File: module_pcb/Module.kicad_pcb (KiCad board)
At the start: 2 copper layers, 44.4 x 52.7 mm, 29 parts, among them J1 L_SIG_CONN, J2 R_PWR_CONN, J3 R_SIG_CONN, J4 L_PWR_CONN, U1 AMS1117-3.3, U2 TBD62783AFNG, U3 SN74HC595PWR, U4 AMS1117-1.5

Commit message: Layout done
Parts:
- removed H2: MountingHole_Pad, MountingHole:MountingHole_3.2mm_M3_ISO14580_Pad_TopBottom
- moved H3 36.3 mm to (146.3, 110.3)
- moved D2 4.40 mm to (157.5, 96.0)
- moved H1 0.78 mm to (146.3, 82.8)
- moved H4 0.55 mm to (183.2, 82.8)
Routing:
- net Vanode: track 2.61 -> 46.2 mm, vias 0 -> 1
- net Net-(U2-O7): track 0.00 -> 37.7 mm, vias 0 -> 1
- net Net-(U2-O5): track 0.00 -> 36.5 mm, vias 0 -> 1
- net Net-(U2-O2): track 0.00 -> 34.6 mm, vias 0 -> 1
- net Net-(U2-O1): track 0.00 -> 33.6 mm, vias 0 -> 2
- net /GRID_1: track 21.2 -> 52.2 mm, vias 1 -> 3
- net Net-(U2-O8): track 0.00 -> 29.6 mm, vias 0 -> 2
- net /SRCLK: track 25.8 -> 55.3 mm, vias 0 -> 1
- net Net-(U2-O6): track 0.00 -> 28.0 mm, vias 0 -> 2
- net Net-(U2-O4): track 0.00 -> 26.8 mm, vias 0 -> 2
- net Net-(U2-O3): track 0.00 -> 26.2 mm
- net /GRID_2: track 28.0 -> 50.5 mm
- net /RCLK: track 19.1 -> 41.6 mm
- net //SRCLR: track 21.2 -> 41.9 mm, vias 1 -> 2
- net /SER: track 27.3 -> 47.6 mm, vias 1 -> 2
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
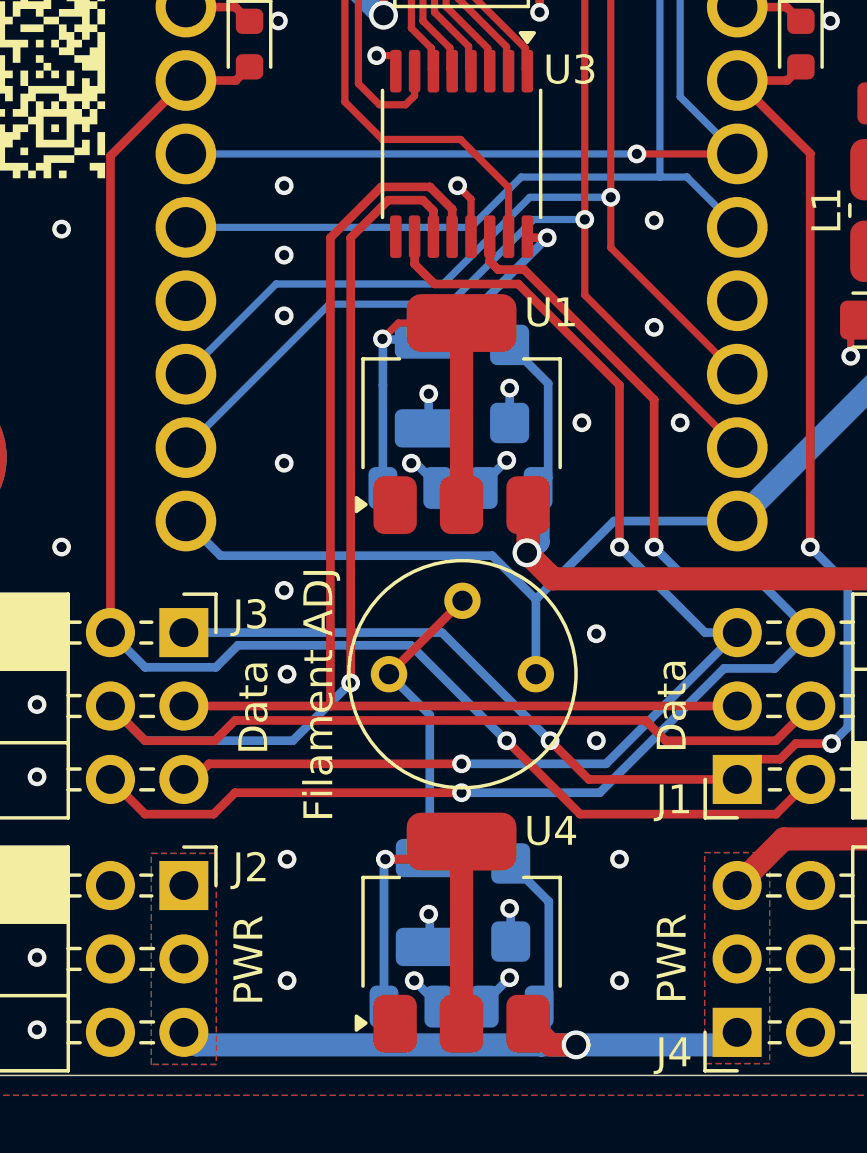
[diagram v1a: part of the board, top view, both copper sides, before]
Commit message: Moved cell battery, generated STEP files
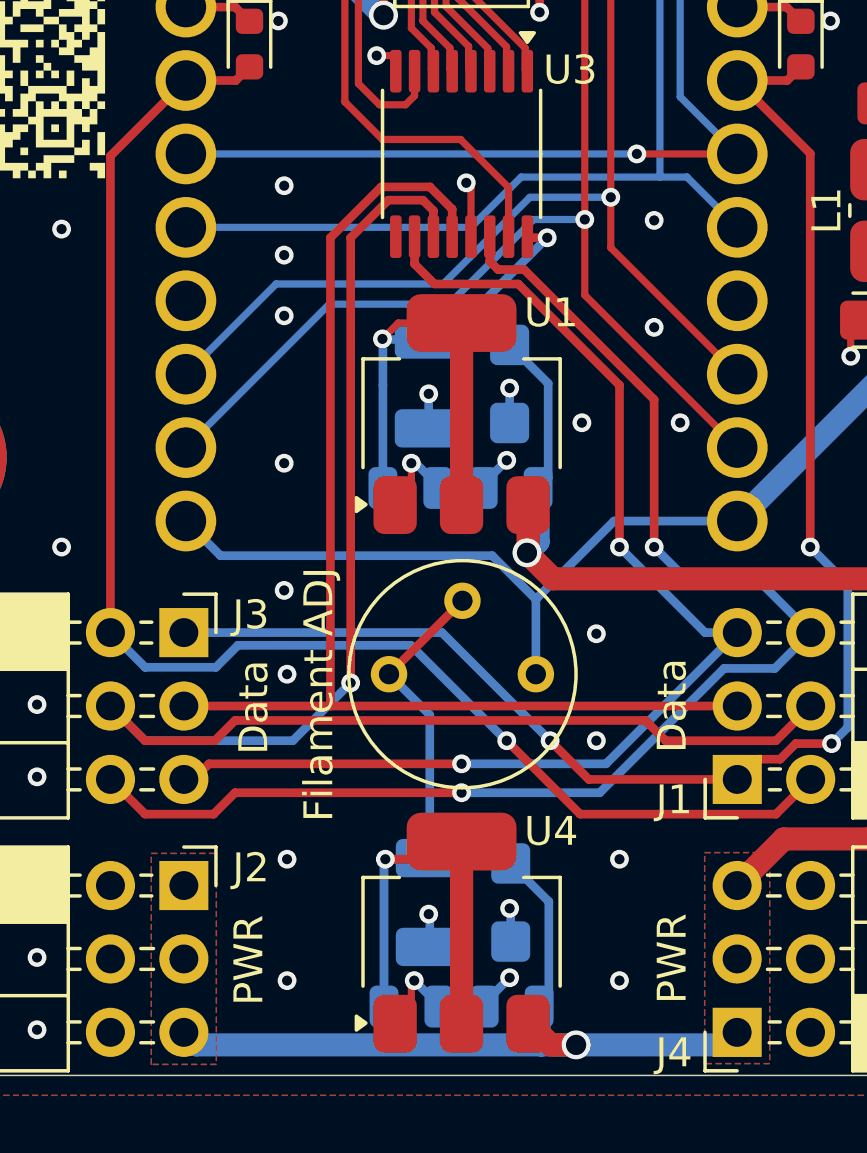
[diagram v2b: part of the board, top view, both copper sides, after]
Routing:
- net GND: track 20.3 -> 23.7 mm
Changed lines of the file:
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@@
+	)
+	(segment
+		(start 162.5375 129.89)
+		(end 163.1 129.3275)
+		(width 0.25)
+		(layer "F.Cu")
+		(net 1)
+	)
+	(segment
+		(start 163.1 129.3275)
+		(end 163.1 128.5)
+		(width 0.25)
+		(layer "F.Cu")
+		(net 1)
 	)
 	(segment
@@
 	)
 	(segment
+		(start 163.1 111.3875)
+		(end 163.1 110.5)
+		(width 0.25)
+		(layer "F.Cu")
+		(net 1)
+	)
+	(segment
 		(start 167.5375 93.94)
 		(end 167.5375 94.9)
@@
 	)
 	(segment
-		(start 165.1625 102.6625)
-		(end 165.1625 101.3625)
+		(start 165.1625 100.9625)
+		(end 165 100.8)
 		(width 0.25)
 		(layer "F.Cu")
@@
 	)
 	(segment
+		(start 162.5375 111.95)
+		(end 163.1 111.3875)
+		(width 0.25)
+		(layer "F.Cu")
+		(net 1)
+	)
+	(segment
 		(start 176.0825 94.72)
 		(end 176.575 95.2125)
@@
 	)
 	(segment
+		(start 163.1 128.5)
+		(end 163.2 128.4)
+		(width 0.25)
+		(layer "F.Cu")
+		(net 1)
+	)
+	(segment
+		(start 165.1625 102.6625)
+		(end 165.1625 100.9625)
+		(width 0.25)
+		(layer "F.Cu")
+		(net 1)
+	)
+	(segment
 		(start 178.3 106.8)
 		(end 178.3 105.88)
-		(width 0.25)
-		(layer "F.Cu")
-		(net 1)
-	)
-	(segment
-		(start 165.1625 101.3625)
-		(end 164.7 100.9)
 		(width 0.25)
 		(layer "F.Cu")
@@
 	)
 	(via
-		(at 164.7 100.9)
-		(size 0.65)
-		(drill 0.35)
+		(at 165 100.8)
+		(size 0.65)
+		(drill 0.35)

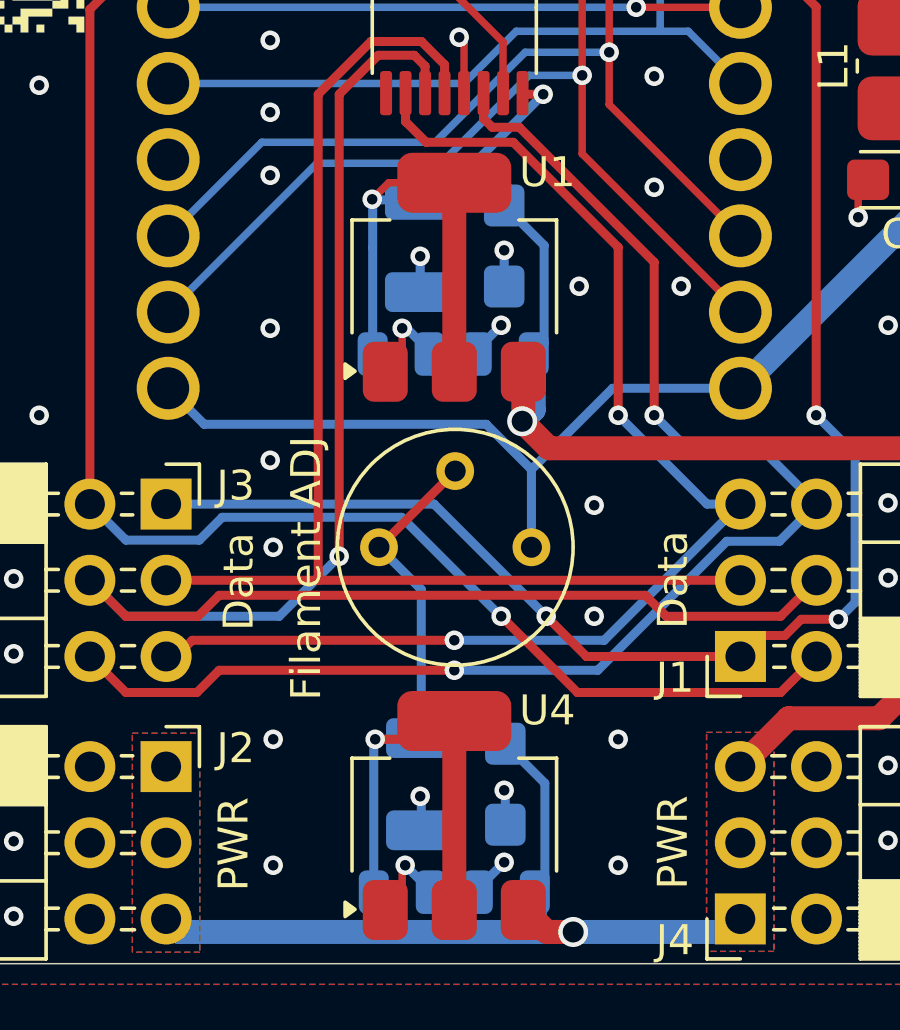
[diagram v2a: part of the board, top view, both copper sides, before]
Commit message: Replaced capacitor footprint with EIA-3216
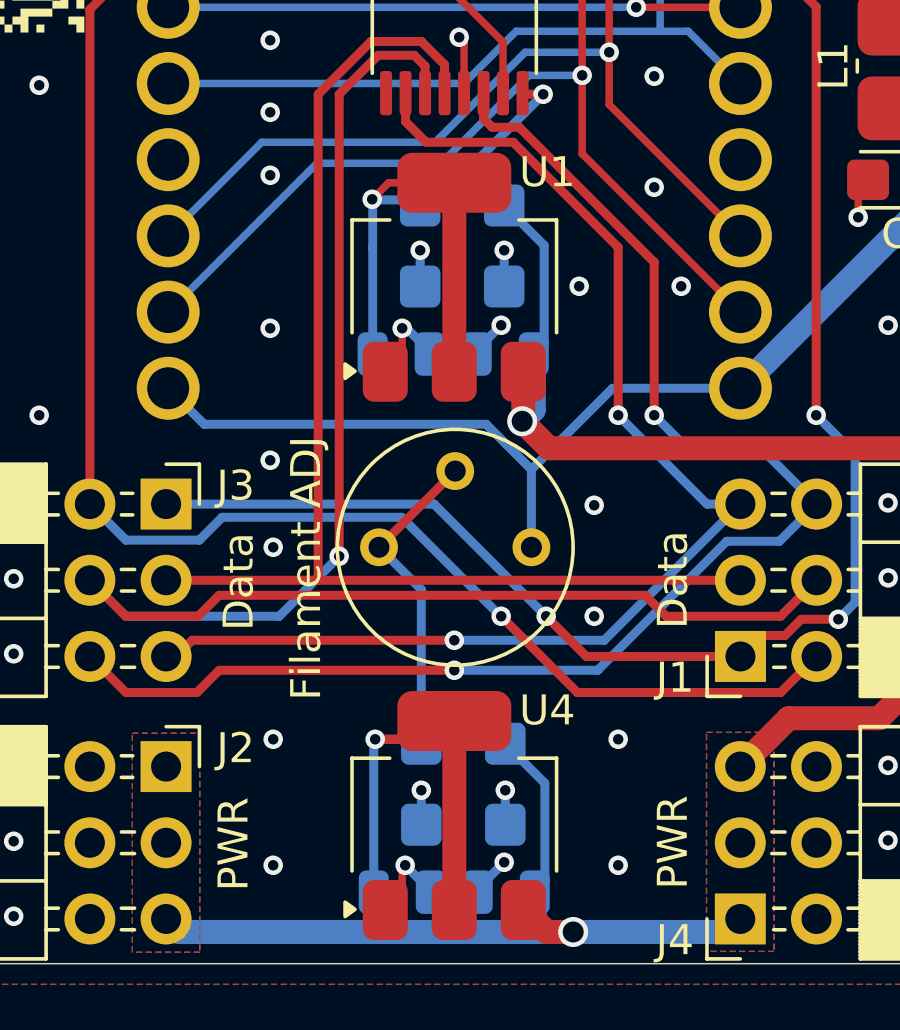
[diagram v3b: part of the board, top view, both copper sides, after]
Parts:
- removed H4: MountingHole_Pad, MountingHole:MountingHole_3.2mm_M3_ISO14580_Pad_TopBottom
- added H2: MountingHole_Pad, MountingHole:MountingHole_3.2mm_M3_ISO14580_Pad_TopBottom, F.Cu at (183.2, 82.8)
- C3, C9: footprint Capacitor_Tantalum_SMD:CP_EIA-3528-15_AVX-H -> Capacitor_Tantalum_SMD:CP_EIA-3216-18_Kemet-A
